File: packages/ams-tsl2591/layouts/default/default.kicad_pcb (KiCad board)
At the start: 2 copper layers, 4 parts

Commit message: Clean PR: Only include packages from package-todos.md
- Updated layouts and parts for packages listed in package-todos.md only
- Includes adi-ad5693r, adi-adbms6822, adi-adbms6830, adi-adxl375, adi-ltc4316
- Updated ams-tsl2591, aosong-aht20, bosch sensors, diodes-inc, espressif
- Updated infineon, invensense, issi, liteon, macroblock, maxim components
- Updated memsic, microchip, rohm, nxp, opsco, st, ti, usb-connectors
- Renamed pjrc-teensy_4_1 to pjrc-teensy-4-1 (hyphen naming convention)
- Updated realtek-rtl8305nb

Removed 64+ packages that were not listed in package-todos.md to keep
PR focused only on packages that are being tracked for review.
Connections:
- net VDD renamed VCC
- net gnd renamed GND
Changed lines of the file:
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@@
     (net 0 "")
     (net 1 "INT")
-    (net 2 "gnd")
+    (net 2 "GND")
     (net 3 "SDA")
     (net 4 "SCL")
     (net 5 "net")
-    (net 6 "VDD")
+    (net 6 "VCC")
     (footprint "Advanced_Monolithic_Systems_TSL25911FN:DFN-6_L2.4-W2.0-P0.65-BL"
         (layer "F.Cu")
         (at 31.35 35.4 90)
         (property "Reference" "U1"
-            (at 0 -4.8 90)
+            (at 0 -4.8 0)
             (layer "F.SilkS")
             (hide yes)
@@
         )
         (property "Value" ""
-            (at 0 4.8 90)
+            (at 0 4.8 0)
             (layer "F.Fab")
             (hide no)
@@
         )
         (property "checksum" "a27bf9a7d529974663251dacaa404faa1e2065c11f8c486d3b080aa925f4c663"
-            (at 0 0 90)
-            (layer "User.9")
-            (hide yes)
-            (effects
-                (font
-                    (size 0.125 0.125)
-                    (thickness 0.01875)
-                )
-            )
-        )
-        (property "__atopile_lib_fp_hash__" "047c179d-bae1-9938-b20f-a5c06e39b00c"
-            (at 0 0 90)
+            (at 0 0 0)
+            (layer "User.9")
+            (hide no)
+            (effects
+                (font
+                    (size 0.125 0.125)
+                    (thickness 0.01875)
+                )
+                (hide yes)
+            )
+        )
+        (property "__atopile_lib_fp_hash__" "dbc4a2e9-fa43-bbef-10b6-508abb206959"
+            (at 0 0 0)
             (layer "User.9")
             (hide yes)
@@
         )
         (attr smd)
+        (fp_line
+            (start -1.03 1)
+            (end -1.2 1)
+            (stroke
+                (width 0.15)
+                (type solid)
+            )
+            (layer "F.SilkS")
+        )
+        (fp_line
+            (start 1.04 -1)
+            (end 1.2 -1)
+            (stroke
+                (width 0.15)
+                (type solid)
+            )
+            (layer "F.SilkS")
+        )
         (fp_line
             (start 1.2 -1)
@@
         )
         (fp_line
-            (start 1.04 -1)
-            (end 1.2 -1)
+            (start 1.2 1)
+            (end 1.04 1)
+            (stroke
+                (width 0.15)
+                (type solid)
+            )
+            (layer "F.SilkS")
+        )
+        (fp_line
+            (start -1.2 1)
+            (end -1.2 -1)
             (stroke
                 (width 0.15)
@@
             (layer "F.SilkS")
         )
-        (fp_line
-            (start 1.2 1)
-            (end 1.04 1)
-            (stroke
-                (width 0.15)
-                (type solid)
-            )
-            (layer "F.SilkS")
-        )
-        (fp_line
-            (start -1.03 1)
-            (end -1.2 1)
-            (stroke
-                (width 0.15)
-                (type solid)
-            )
-            (layer "F.SilkS")
-        )
-        (fp_line
-            (start -1.2 1)
-            (end -1.2 -1)
-            (stroke
-                (width 0.15)
-                (type solid)
-            )
-            (layer "F.SilkS")
+        (fp_circle
+            (center -1.2 1)
+            (end -1.17 1)
+            (stroke
+                (width 0.06)
+                (type solid)
+            )
+            (fill no)
+            (layer "F.Fab")
+        )
+        (fp_circle
+            (center -0.65 1.32)
+            (end -0.53 1.32)
+            (stroke
+                (width 0.24)
+                (type solid)
+            )
+            (fill no)
+            (layer "Cmts.User")
         )
         (fp_circle
@@
             (layer "F.SilkS")
         )
-        (fp_circle
-            (center -0.65 1.32)
-            (end -0.53 1.32)
-            (stroke
-                (width 0.24)
-                (type solid)
-            )
-            (fill no)
-            (layer "Cmts.User")
-        )
-        (fp_circle
-            (center -1.2 1)
-            (end -1.17 1)
-            (stroke
-                (width 0.06)
-                (type solid)
-            )
-            (fill no)
-            (layer "F.Fab")
+        (fp_text user "%R"
+            (at 0 0 0)
+            (layer "F.Fab")
+            (effects
+                (font
+                    (size 1 1)
+                    (thickness 0.15)
+                )
+            )
+            (unlocked no)
         )
         (fp_text user "${REFERENCE}"
-            (at 0 -4.8 90)
-            (layer "F.SilkS")
-            (effects
-                (font
-                    (size 1 1)
-                    (thickness 0.15)
-                )
-                (hide yes)
-            )
-            (unlocked no)
-        )
-        (fp_text user "${REFERENCE}"
-            (at 0 0 90)
-            (layer "F.Fab")
+            (at 0 -4.8 0)
+            (layer "F.SilkS")
             (effects
                 (font
@@
             (at -0.65 0.8 90)
             (size 0.4 1.1)
-            (layers "F.Cu" "F.Mask" "F.Paste")
+            (layers "F.Cu" "F.Paste" "F.Mask")
             (net 4 "SCL")
         )
@@
             (at 0 0.8 90)
             (size 0.4 1.1)
-            (layers "F.Cu" "F.Mask" "F.Paste")
+            (layers "F.Cu" "F.Paste" "F.Mask")
             (net 1 "INT")
         )
@@
             (at 0.65 0.8 90)
             (size 0.4 1.1)
-            (layers "F.Cu" "F.Mask" "F.Paste")
-            (net 2 "gnd")
+            (layers "F.Cu" "F.Paste" "F.Mask")
+            (net 2 "GND")
         )
         (pad "4" smd rect
             (at 0.65 -0.8 90)
             (size 0.4 1.1)
-            (layers "F.Cu" "F.Mask" "F.Paste")
+            (layers "F.Cu" "F.Paste" "F.Mask")
             (net 5 "net")
         )
@@
             (at 0 -0.8 90)
             (size 0.4 1.1)
-            (layers "F.Cu" "F.Mask" "F.Paste")
-            (net 6 "VDD")
+            (layers "F.Cu" "F.Paste" "F.Mask")
+            (net 6 "VCC")
         )
         (pad "6" smd rect
             (at -0.65 -0.8 90)
             (size 0.4 1.1)
-            (layers "F.Cu" "F.Mask" "F.Paste")
+            (layers "F.Cu" "F.Paste" "F.Mask")
             (net 3 "SDA")
         )
-        (embedded_fonts no)
         (model "${KIPRJMOD}/../../parts/Advanced_Monolithic_Systems_TSL25911FN/DFN-6_L2.4-W2.0-P0.65-BL.step"
             (offset
@@
             )
         )
-        (property "__atopile_lib_fp_hash__" "b1c3d7ac-ef7b-aa3f-ccae-b4e8b3bd5565"
+        (property "__atopile_lib_fp_hash__" "ac993d00-cd2e-9909-323a-aafc825a9032"
             (at 0 0 0)
             (layer "User.9")
@@
             (size 0.57 0.54)
             (layers "F.Cu" "F.Paste" "F.Mask")
-            (net 6 "VDD")
+            (net 6 "VCC")
         )
         (pad "1" smd rect
@@
             )
         )
-        (property "__atopile_lib_fp_hash__" "56073f1d-294d-1420-a144-b16ab845bfe9"
+        (property "__atopile_lib_fp_hash__" "77ce5adf-3702-77eb-5a03-81a966899838"
             (at 0 0 0)
             (layer "User.9")
@@
             (size 0.79 0.54)
             (layers "F.Cu" "F.Paste" "F.Mask")
-            (net 2 "gnd")
+            (net 2 "GND")
         )
         (pad "1" smd rect
@@
             (size 0.79 0.54)
             (layers "F.Cu" "F.Paste" "F.Mask")
-            (net 6 "VDD")
+            (net 6 "VCC")
         )
         (model "${KIPRJMOD}/../../parts/Samsung_Electro_Mechanics_CL05A105KA5NQNC/C0402_L1.0-W0.5-H0.5.step"
@@
             )
         )
-        (property "__atopile_lib_fp_hash__" "b1c3d7ac-ef7b-aa3f-ccae-b4e8b3bd5565"
+        (property "__atopile_lib_fp_hash__" "ac993d00-cd2e-9909-323a-aafc825a9032"
             (at 0 0 0)
             (layer "User.9")
@@
             (size 0.57 0.54)
             (layers "F.Cu" "F.Paste" "F.Mask")
-            (net 6 "VDD")
+            (net 6 "VCC")
         )
         (pad "1" smd rect

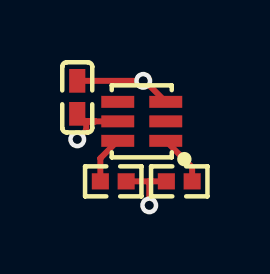
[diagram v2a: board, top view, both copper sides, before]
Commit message: ams-tsl2591: package update [reviewer:Narayan Powderly] [ato:^0.14.0] (#225)
* ams-tsl2591: package update to v0.2.0, ato:^0.14.0

Build targets:
  default = rc0
  usage = rc0
Package Verify: rc0
Version: 0.1.1 -> 0.2.0
Requires ato: ^0.14.0

* Update main.yml to match feature/0.14-compatibility

Syncs GitHub Actions workflow configuration for 0.14.x compatibility.
Uses setup-atopile@v1.8 with docker-tag feature-fabll_part2.

* ci: update workflow from main (fix package publish git issue)

* ams-tsl2591: sync build outputs

Build targets:
  default = rc0
  usage = rc0
Package Verify: rc0

---------

Co-authored-by: Nicholas Krstevski <nick@atopile.io>
Co-authored-by: Nick Krstevski <51719418+nickkrstevski@users.noreply.github.com>
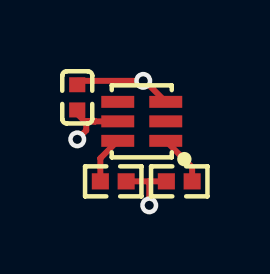
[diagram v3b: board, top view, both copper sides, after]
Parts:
- C1: value 1µF ±10% 25V X5R -> {8.999..1.1}F
- R1, R2: value 10kΩ ±1% 62.5mW -> 10000±1.0%Ω
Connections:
- net GND renamed lv
- net VCC renamed hv
- U1 pad 4: net -> (no net)
